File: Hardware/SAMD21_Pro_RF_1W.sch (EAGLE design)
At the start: 70 parts, among them J10 AVR_SPI_PROG_3X2TESTPOINTS, J12 5.5x2.1mm Barrel, J13 U.FL, J7 PTH, J9 External On/Off, Q1 310mA/60V/1.6Ω, U1 MCP73831, U3 3.3V, U4 ATSAMD21G, U5 4MB Flash, U6 E19-915MS1W, U7 ADJ5, U8 TXB0108DQSR, Y1 32.768kHz

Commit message: Stuff
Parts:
- R14: value 750K -> 750; device SparkFun-Resistors:750KOHM-0603-1/10W-1% -> SparkFun-Resistors:750OHM-0603-1/10W-1%
- R5: value 2.0k -> 2.2k; device SparkFun-Resistors:2.0KOHM-0603-1/10W-5% -> SparkFun-Resistors:2.2KOHM-0603-1/10W-1%
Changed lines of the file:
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@@
 <?xml version="1.0" encoding="utf-8"?>
 <!DOCTYPE eagle SYSTEM "eagle.dtd">
-<eagle version="9.0.1">
+<eagle version="9.1.3">
 <drawing>
 <settings>
@@
 <part name="GND10" library="supply1" library_urn="urn:adsk.eagle:library:371" deviceset="GND" device=""/>
 <part name="U1" library="SparkFun-IC-Power" deviceset="MCP73831" device=""/>
-<part name="R5" library="SparkFun-Resistors" deviceset="2.0KOHM" device="-0603-1/10W-5%" value="2.0k"/>
+<part name="R5" library="SparkFun-Resistors" deviceset="2.2KOHM" device="-0603-1/10W-1%" value="2.2k"/>
 <part name="GND14" library="supply1" library_urn="urn:adsk.eagle:library:371" deviceset="GND" device=""/>
 <part name="GND17" library="supply1" library_urn="urn:adsk.eagle:library:371" deviceset="GND" device=""/>
@@
 <part name="U7" library="SparkFun-IC-Power" deviceset="V_REG_LM1117" device="SOT223" value="ADJ5"/>
 <part name="F1" library="SparkFun-Fuses" deviceset="PPTC" device="_6V500MA" value="6V 0.5A"/>
-<part name="R14" library="SparkFun-Resistors" deviceset="750KOHM" device="-0603-1/10W-1%" value="750K"/>
+<part name="R14" library="SparkFun-Resistors" deviceset="750OHM" device="-0603-1/10W-1%" value="750"/>
 <part name="R15" library="SparkFun-Resistors" deviceset="240OHM" device="-0603-1/10W-1%" value="240"/>
 <part name="GND33" library="SparkFun" deviceset="GND" device=""/>

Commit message: Finalizing things
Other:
- note added: "Max Voltage Input: 7VDC"
- note removed: "Max Voltage Input: 20VDC"
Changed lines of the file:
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@@
 <text x="76.2" y="86.36" size="2.54" layer="94" font="vector">RX/TX LEDs</text>
 <text x="388.62" y="226.06" size="1.778" layer="97" font="vector" rot="R180">Reset occurs when low</text>
-<text x="218.44" y="274.32" size="1.778" layer="97" font="vector">Max Voltage Input: 20VDC</text>
+<text x="218.44" y="274.32" size="1.778" layer="97" font="vector">Max Voltage Input: 7VDC</text>
 <text x="218.44" y="271.78" size="1.778" layer="97" font="vector">Max Current Output: 800mA</text>
 <wire x1="294.64" y1="144.78" x2="294.64" y2="218.44" width="0.2032" layer="97" style="shortdash"/>
@@
 <text x="299.72" y="210.82" size="2.54" layer="94" font="vector">Level Shifters</text>
 <text x="160.02" y="256.54" size="1.27" layer="97">VIN 7-15V</text>
+<text x="190.5" y="93.98" size="1.778" layer="97" font="vector">Max Voltage Input: 7VDC</text>
 </plain>
 <instances>

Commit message: x02
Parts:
- removed J15, J2: (no value), SparkFun-Connectors:QWIIC_CONNECTORJS-1MM
- removed LED1: RED, SparkFun-LED:LED-RED0603
- removed R15: 240, SparkFun-Resistors:240OHM-0603-1/10W-1%
- removed R16: 10k, SparkFun-Resistors:10KOHM-0603-1/10W-1%
- removed S3: MOMENTARY-SWITCH-SPST-SMD-RIGHT-ANGLE, SparkFun-Switches:MOMENTARY-SWITCH-SPST-SMD-RIGHT-ANGLE
- removed U$26: SPECIAL_INSTRUCTIONS-ORDERING, SparkFun-Aesthetics:SPECIAL_INSTRUCTIONS-ORDERING
- removed U7: ADJ5, SparkFun-IC-Power:V_REG_LM1117SOT223
- removed U8: TXB0108DQSR, SparkFun-IC-Comms:TXB0108
- added D2: Green, SparkFun-LED:LED-GREEN0603
- added J14: CORTEX_DEBUG_PTH, SparkFun-Connectors:CORTEX_DEBUG_PTH
- added Q2: 310mA/60V/1.6Ω, SparkFun-DiscreteSemi:MOSFET-NCH-2N7002PW
- added R11: 10k, SparkFun-Resistors:10KOHM-0603-1/10W-1%
- added R3, R4: 1k, SparkFun-Resistors:1KOHM-0603-1/10W-1%
- added S2: Power, SparkFun-Switches:SWITCH-SPDT-SMD-RIGHT-ANGLE
- added U2: 3.3V, SparkFun-IC-Power:V_REG_AP2112K-3.3V
- C1: value 10uF -> 15pF; device SparkFun-Capacitors:10UF-POLAR-EIA3216-16V-10%(TANT) -> SparkFun-Capacitors:15PF-0603-50V-5%
- C10: value 0.1uF -> 10uF; device SparkFun-Capacitors:0.1UF-0603-25V-(+80/-20%) -> SparkFun-Capacitors:10UF-POLAR-EIA3216-16V-10%(TANT)
- C11, C14: value 0.1uF -> 1.0uF; device SparkFun-Capacitors:0.1UF-0603-25V-(+80/-20%) -> SparkFun-Capacitors:1.0UF-0603-16V-10%
- C12: value 1.0uF -> 10uF; device SparkFun-Capacitors:1.0UF-0603-16V-10% -> SparkFun-Capacitors:10UF-POLAR-EIA3216-16V-10%(TANT)
- C13, C7: value 10uF -> 0.1uF; device SparkFun-Capacitors:10UF-POLAR-EIA3216-16V-10%(TANT) -> SparkFun-Capacitors:0.1UF-0603-25V-(+80/-20%)
- C3: value 15pF -> 0.1uF; device SparkFun-Capacitors:15PF-0603-50V-5% -> SparkFun-Capacitors:0.1UF-0603-25V-(+80/-20%)
- C5: value 1.0uF -> 0.1uF; device SparkFun-Capacitors:1.0UF-0603-16V-10% -> SparkFun-Capacitors:0.1UF-0603-25V-(+80/-20%)
- C8: value 0.1uF -> 4.7uF; device SparkFun-Capacitors:0.1UF-0603-25V-(+80/-20%) -> SparkFun-Capacitors:4.7UF-0603-6.3V-(10%)
- C9: value 4.7uF -> 10uF; device SparkFun-Capacitors:4.7UF-0603-6.3V-(10%) -> SparkFun-Capacitors:10UF-POLAR-EIA3216-16V-10%(TANT)
- D1: value Green -> Yellow; device SparkFun-LED:LED-GREEN0603 -> SparkFun-LED:LED-YELLOW0603
- D3: value 3A/10V/300mV -> BLUE; device SAMD21_ProRF_1W:DIODE-SCHOTTKY-BAT60A -> SparkFun-LED:LED-BLUE0603
- D4: value BLUE -> 3A/10V/300mV; device SparkFun-LED:LED-BLUE0603 -> SAMD21_ProRF_1W:DIODE-SCHOTTKY-BAT60A
- D6: value Yellow -> RED; device SparkFun-LED:LED-YELLOW0603 -> SparkFun-LED:LED-RED0603
- J10: value AVR_SPI_PROG_3X2TESTPOINTS -> (none); device SparkFun-Connectors:AVR_SPI_PROG_3X2TESTPOINTS -> SparkFun-Connectors:CONN_10NO_SILK_PTH_FEMALE
- J11: device SparkFun-Connectors:CONN_09NO_SILK -> SparkFun-Connectors:QWIIC_CONNECTORJS-1MM
- J12: value 5.5x2.1mm Barrel -> (none); device SparkFun-Connectors:POWER_JACKSMD -> SparkFun-Connectors:CONN_01PTH_NO_SILK_YES_STOP
- J13: value U.FL -> (none); device SparkFun-Connectors:U.FL -> SparkFun-Connectors:QWIIC_CONNECTORJS-1MM
- J3: value (none) -> PTH; device SparkFun-Connectors:CONN_10NO_SILK_PTH_FEMALE -> SparkFun-Connectors:CONN_021X02_NO_SILK
- J4: device SparkFun-Connectors:CONN_01PTH_NO_SILK_YES_STOP -> SparkFun-Connectors:CONN_021X02_NO_SILK
- J5: value (none) -> 5.5x2.1mm Barrel; device SparkFun-Connectors:CONN_09NO_SILK -> SparkFun-Connectors:POWER_JACKSMD
- J7: value PTH -> (none); device SparkFun-Connectors:CONN_021X02_NO_SILK -> SparkFun-Connectors:CONN_09NO_SILK
- J8: value (none) -> External On/Off
- J9: value External On/Off -> (none); device SparkFun-Connectors:CONN_021X02_NO_SILK -> SparkFun-Connectors:CONN_09NO_SILK
- R10, R7, R9: value 1k -> 10k; device SparkFun-Resistors:1KOHM-0603-1/10W-1% -> SparkFun-Resistors:10KOHM-0603-1/10W-1%
- R13: value 1k -> 2.2k; device SparkFun-Resistors:1KOHM-0603-1/10W-1% -> SparkFun-Resistors:2.2KOHM-0603-1/10W-1%
- R14: value 750 -> 2.2k; device SparkFun-Resistors:750OHM-0603-1/10W-1% -> SparkFun-Resistors:2.2KOHM-0603-1/10W-1%
- R2, R8: value 10k -> 1k; device SparkFun-Resistors:10KOHM-0603-1/10W-1% -> SparkFun-Resistors:1KOHM-0603-1/10W-1%
- R5: value 2.2k -> 240; device SparkFun-Resistors:2.2KOHM-0603-1/10W-1% -> SparkFun-Resistors:240OHM-0603-1/10W-1%
- R6: value 10k -> 750; device SparkFun-Resistors:10KOHM-0603-1/10W-1% -> SparkFun-Resistors:750OHM-0603-1/10W-1%
- S1: value Power -> MOMENTARY-SWITCH-SPST-SMD-5.2-REDUNDANT; device SparkFun-Switches:SWITCH-SPDT-SMD-RIGHT-ANGLE -> SparkFun-Switches:MOMENTARY-SWITCH-SPST-SMD-5.2-REDUNDANT
- U1: value MCP73831 -> ATSAMD21G; device SparkFun-IC-Power:MCP73831 -> temp:ATSAMD21G
- U3: value 3.3V -> ADJ5; device SparkFun-IC-Power:V_REG_AP2112K-3.3V -> SparkFun-IC-Power:V_REG_LM1117SOT223
- U4: value ATSAMD21G -> 4MB Flash; device temp:ATSAMD21G -> SparkFun-IC-Memory:AT25SF041
- U5: value 4MB Flash -> E19-915MS1W; device SparkFun-IC-Memory:AT25SF041 -> SAMD21_ProRF_1W:E19-915MS1W
- U6: value E19-915MS1W -> TXB0108DQSR; device SAMD21_ProRF_1W:E19-915MS1W -> SparkFun-IC-Comms:TXB0108
- renumbered FRAME2 to FRAME1
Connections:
- removed net CHARGE_STAT: R9.1, U1.STAT
- removed net D2: J3.6, U4.PA14(XIN/SER2:2+)_D2
- removed net D3: J3.5, U4.PA09(I2C/AIN17/SER0:1+)_D3
- removed net D4: J3.4, U4.PA08(I2C/AIN16/SER0:0+)_D4
- removed net E19_RST: U4.PA17(I2C/SER1:1+)_D13, U6.!RST
- removed net N$11: R5.1, U1.PROG
- removed net N$8: D4.C, R9.2
- removed net N$9: J9.2, S1.O
- removed net VBATT_LVL: R1.1, R2.2, U4.A5_PB02(AIN10/SER5:0)
- new net !E19_RST: Q1.S, R9.1, U1.PA13(I2C/SER2:1+)
- new net !E19_RST5V: Q1.D, R11.1, U5.!RST
- new net D13: R4.2, U1.PA17(I2C/SER1:1+)_D13
- new net EEPROM_MISO: J6.6, U1.PA14(XIN/SER2:2+)_D2, U4.SO(D1)
- new net EEPROM_MOSI: J6.4, U1.PA08(I2C/AIN16/SER0:0+)_D4, U4.SI(D0)
- new net EEPROM_SCLK: J6.5, U1.PA09(I2C/AIN17/SER0:1+)_D3, U4.SCK
- new net N$3: D3.A, R4.1
- net !E19_CS: now also Q2.S, R10.1, U1.PA19(SER1:3+)_D12; no longer Q1.S, R12.1, U4.PA19(SER1:3+)_D12
- net !E19_CS5V: now also Q2.D, R12.1, U5.!NSS; no longer Q1.D, R16.1, U6.!NSS
- net !RST: now also J14.!RESET, J6.8, R1.1, S1.2, U1.!RESET!; no longer J10.5, J3.8, R6.1, S3.1, U4.!RESET!
- net 3.3V: now also C10.+, C11.1, C13.2, C5.2, D2.A, J11.2, J13.2, J14.VCC, J6.2, Q2.G, R1.2, R10.2, R14.2, R7.2, R9.2, U1.VDDCORE, U1.VDDIN, U1.VDDIO@17, U1.VDDIO@36, U2.OUT, U4.!HOLD(D3), U4.!WP(D2), U4.VCC, U6.OE, U6.VCCA; no longer C10.2, C12.1, C13.+, C14.2, D6.A, J10.2, J15.2, J2.2, J3.2, R12.2, R6.2, U3.OUT, U4.VDDCORE, U4.VDDIN, U4.VDDIO@17, U4.VDDIO@36, U5.!HOLD(D3), U5.!WP(D2), U5.VCC, U8.OE, U8.VCCA
- net 5V: now also C12.+, C14.1, C15.2, D4.C, R11.2, R12.2, U2.EN, U2.IN, U5.VCC, U6.VCCB; no longer C5.1, C7.+, C8.2, D3.C, R16.2, U3.EN, U3.IN, U6.VCC, U8.VCCB
- net A0: now also J7.9, U1.A0_PA02(AIN0/DAC); no longer J11.9, U4.A0_PA02(AIN0/DAC)
- net A1: now also J7.8, U1.A1_PB08(AIN2/SER4:0/TC4:0); no longer J11.8, U4.A1_PB08(AIN2/SER4:0/TC4:0)
- net A2: now also J7.7, U1.A2_PB09(AIN3/SER4:1/TC4:1); no longer J11.7, U4.A2_PB09(AIN3/SER4:1/TC4:1)
- net A3: now also J7.6, U1.A3_PA04(AIN4/REFB/SER0:0/TC0:0); no longer J11.6, U4.A3_PA04(AIN4/REFB/SER0:0/TC0:0)
- net A4: now also J7.5, U1.A4_PA05(AIN5/SER0:1/TC0:1); no longer J11.5, U4.A4_PA05(AIN5/SER0:1/TC0:1)
- net ANT: now also J12.1, U5.ANT; no longer J13.SIGNAL, J4.1, U6.ANT
- net D+: now also U1.PA25(SER3:3+); no longer U4.PA25(SER3:3+)
- net D-: now also U1.PA24(SER3:2+); no longer U4.PA24(SER3:2+)
- net D10: now also U1.PA18(SER1:2+)_D10, U6.A7; no longer U4.PA18(SER1:2+)_D10, U8.A7
- net D11: now also U1.PA16(I2C/SER1:0+)_D11, U6.A8; no longer U4.PA16(I2C/SER1:0+)_D11, U8.A8
- net D5: now also J6.7, U1.PA15(XOUT/SER2:3+)_D5; no longer J3.7, U4.PA15(XOUT/SER2:3+)_D5
- net D8_!FLASH_CS: now also R7.1, U1.D8_PA06(AIN6/SER0:2/TC1:0), U4.!CS; no longer R8.1, U4.D8_PA06(AIN6/SER0:2/TC1:0), U5.!CS
- net D9: now also J6.3, U1.D9_PA07(AIN7/SER0:3/TC1:1); no longer J3.3, U4.D9_PA07(AIN7/SER0:3/TC1:1)
- net DIO05V: now also U5.DIO0, U6.B6; no longer U6.DIO0, U8.B6
- net DIO15V: now also U5.DIO1, U6.B7; no longer U6.DIO1, U8.B7
- net DIO25V: now also U5.DIO2, U6.B8; no longer U6.DIO2, U8.B8
- net E19_INT: now also U1.PA20(SER5:2+)_D6, U6.A6; no longer U4.PA20(SER5:2+)_D6, U8.A6
- net E19_RXEN: now also U1.PB23(SER5:3+), U6.A5; no longer U4.PB23(SER5:3+), U8.A5
- net E19_RXEN5V: now also U5.RXEN, U6.B5; no longer U6.RXEN, U8.B5
- net E19_TXEN: now also U1.PB22(SER5:2+), U6.A4; no longer U4.PB22(SER5:2+), U8.A4
- net E19_TXEN5V: now also U5.TXEN, U6.B4; no longer U6.TXEN, U8.B4
- net GND: now also C1.1, C10.-, C11.2, C12.-, C13.1, C14.2, C5.1, C7.1, C8.2, C9.-, D3.C, D6.C, J10.1, J10.10, J10.2, J10.3, J10.4, J10.5, J10.7, J10.8, J10.9, J13.1, J14.GND@3, J14.GND@5, J3.1, J4.1, J5.GND, J5.GNDBREAK, J9.1, J9.2, J9.3, J9.4, J9.5, J9.6, J9.7, J9.8, J9.9, R6.1, S1.1, U1.GND@18, U1.GND@35, U1.GND@42, U1.GNDANA, U2.GND, U4.GND; no longer C1.-, C10.1, C11.1, C12.2, C13.-, C14.1, C5.2, C7.-, C8.1, C9.2, J12.GND, J12.GNDBREAK, J13.GND@0, J13.GND@1, J15.1, J2.1, J5.1, J5.2, J5.3, J5.4, J5.5, J5.6, J5.7, J5.8, J5.9, J6.1, J6.10, J6.2, J6.3, J6.4, J6.5, J6.6, J6.7, J6.8, J6.9, J8.1, LED1.C, R14.1, R2.1, R5.2, S3.2, U1.VSS, U3.GND, U4.GND@18, U4.GND@35, U4.GND@42, U4.GNDANA, U8.GND
- net MISO: now also J14.SWO/TDO, J7.2, U1.PA12(I2C/SER2:0+)_MISO, U6.A2; no longer J10.1, J11.2, U4.PA12(I2C/SER2:0+)_MISO, U5.SO(D1), U8.A2
- net MISO5V: now also U5.MISO, U6.B2; no longer U6.MISO, U8.B2
- net MOSI: now also J7.3, U1.PB10(SER4:2+)_MOSI, U6.A3; no longer J11.3, U4.PB10(SER4:2+)_MOSI, U5.SI(D0), U8.A3
- net MOSI5V: now also U5.MOSI, U6.B3; no longer U6.MOSI, U8.B3
- net N$1: now also D1.C, R2.2; no longer D6.C, R10.2
- net N$12: now also D4.A; no longer D3.A
- net N$13: now also R5.1, R6.2, U3.ADJ; no longer R14.2, R15.1, U7.ADJ
- net N$14: now also R5.2, U3.OUT, U3.OUT@1; no longer R15.2, U7.OUT, U7.OUT@1
- net N$2: now also D2.C, R3.2; no longer D1.C, R7.2
- net N$38: now also D6.A, R8.1; no longer LED1.A, R13.1
- net N$6: now also C1.2, U1.PA00(XIN32/SER1:0/TC2:0); no longer C2.2, U4.PA00(XIN32/SER1:0/TC2:0)
- net N$7: now also C2.2, U1.PA01(XOUT32/SER1:1/TC2:1); no longer C3.2, U4.PA01(XOUT32/SER1:1/TC2:1)
- net RAW: now also J6.1, J8.1, S2.P, U3.IN; no longer J3.1, J9.1, S1.P, U7.IN
- net RXI: now also J6.10, U1.PA11(AIN19/SER0:3+)_D0/RX; no longer J3.10, U4.PA11(AIN19/SER0:3+)_D0/RX
- net RX_LED: now also R2.1, U1.PB03(AIN11/SER5:1); no longer R10.1, U4.PB03(AIN11/SER5:1)
- net SCK: now also J7.4, U1.PB11(SER4:3+)_SCK, U6.A1; no longer J11.4, U4.PB11(SER4:3+)_SCK, U5.SCK, U8.A1
- net SCK5V: now also U5.SCK, U6.B1; no longer U6.SCK, U8.B1
- net SCL: now also J11.4, J13.4, R14.1, U1.PA23(I2C/SER3:0+)_SCL; no longer J15.4, J2.4, U4.PA23(I2C/SER3:0+)_SCL
- net SDA: now also J11.3, J13.3, R13.1, U1.PA22(I2C/SER3:0+)_SDA; no longer J15.3, J2.3, U4.PA22(I2C/SER3:0+)_SDA
- net SWDCLK: now also J14.SWDCLK/TCK, U1.PA30(SWCLK/SER1:2+); no longer J10.3, U4.PA30(SWCLK/SER1:2+)
- net SWDIO: now also J14.SWDIO/TMS, U1.PA31(SWDIO/SER1:3+); no longer J10.4, U4.PA31(SWDIO/SER1:3+)
- net TXO: now also J6.9, U1.PA10(AIN18/SER0:2+)_D1/TX; no longer J3.9, U4.PA10(AIN18/SER0:2+)_D1/TX
- net TX_LED: now also R3.1, U1.PA27; no longer R7.1, U4.PA27
- net USB_VCC: now also C3.2, C8.1, J4.2; no longer C11.2, C9.1, D4.A, J8.2, U1.VIN
- net VBATT: now also C9.+, J3.2, J5.PWR, J8.2, S2.S; no longer C1.+, J12.PWR, J7.2, R1.2, S1.S, U1.VBAT
- net VDDANA: now also C7.2, U1.VDDANA; no longer C15.2, U4.VDDANA
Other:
- note added: "D2"
- note added: "D3"
- note added: "D4"
- note added: "Max Current Output: 600mA"
- note added: "Max Voltage Input: 15VDC"
- note added: "Max Voltage Input: 6VDC"
- note added: "VUSB"
- note added: "When not using EEPROM you can use these pins as GPIOs D2-D4"
- note added: "x02"
- note removed: "Antenna"
- note removed: "LIPO CHARGER"
- note removed: "Reset occurs when low"
- note removed: "x01"
- moved on the sheet: C11, C14, C15, C2, C3, C4, C5, C6, C8, D1, D6, J6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

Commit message: x02 ready for order
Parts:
- removed LOGO1: OSHW-LOGOMINI, SparkFun-Aesthetics:OSHW-LOGOMINI
- U$34: value SPARKX-LOGO2 -> SPARKX-LOGO4; device SparkX:SPARKX-LOGO2 -> SparkX:SPARKX-LOGO4
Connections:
- net GND: now also J14.GNDDTCT
- net MISO: no longer J14.SWO/TDO

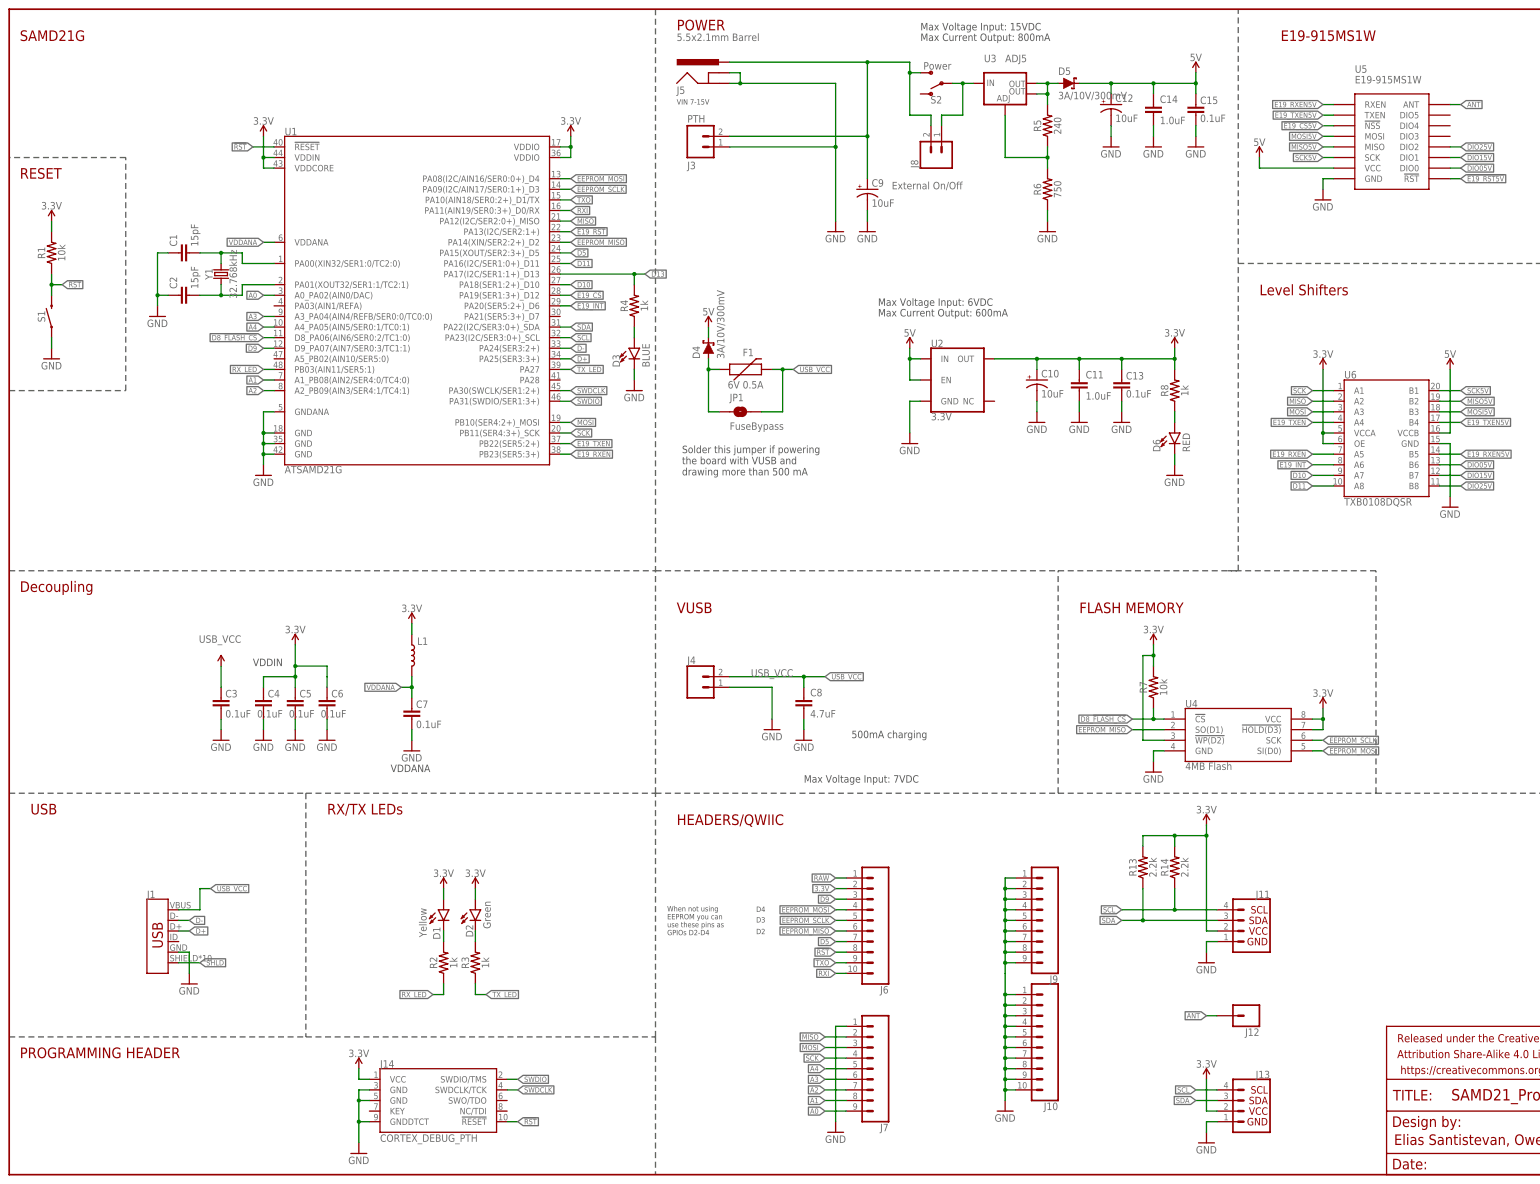
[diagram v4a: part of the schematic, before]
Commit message: Brought libraries into spec
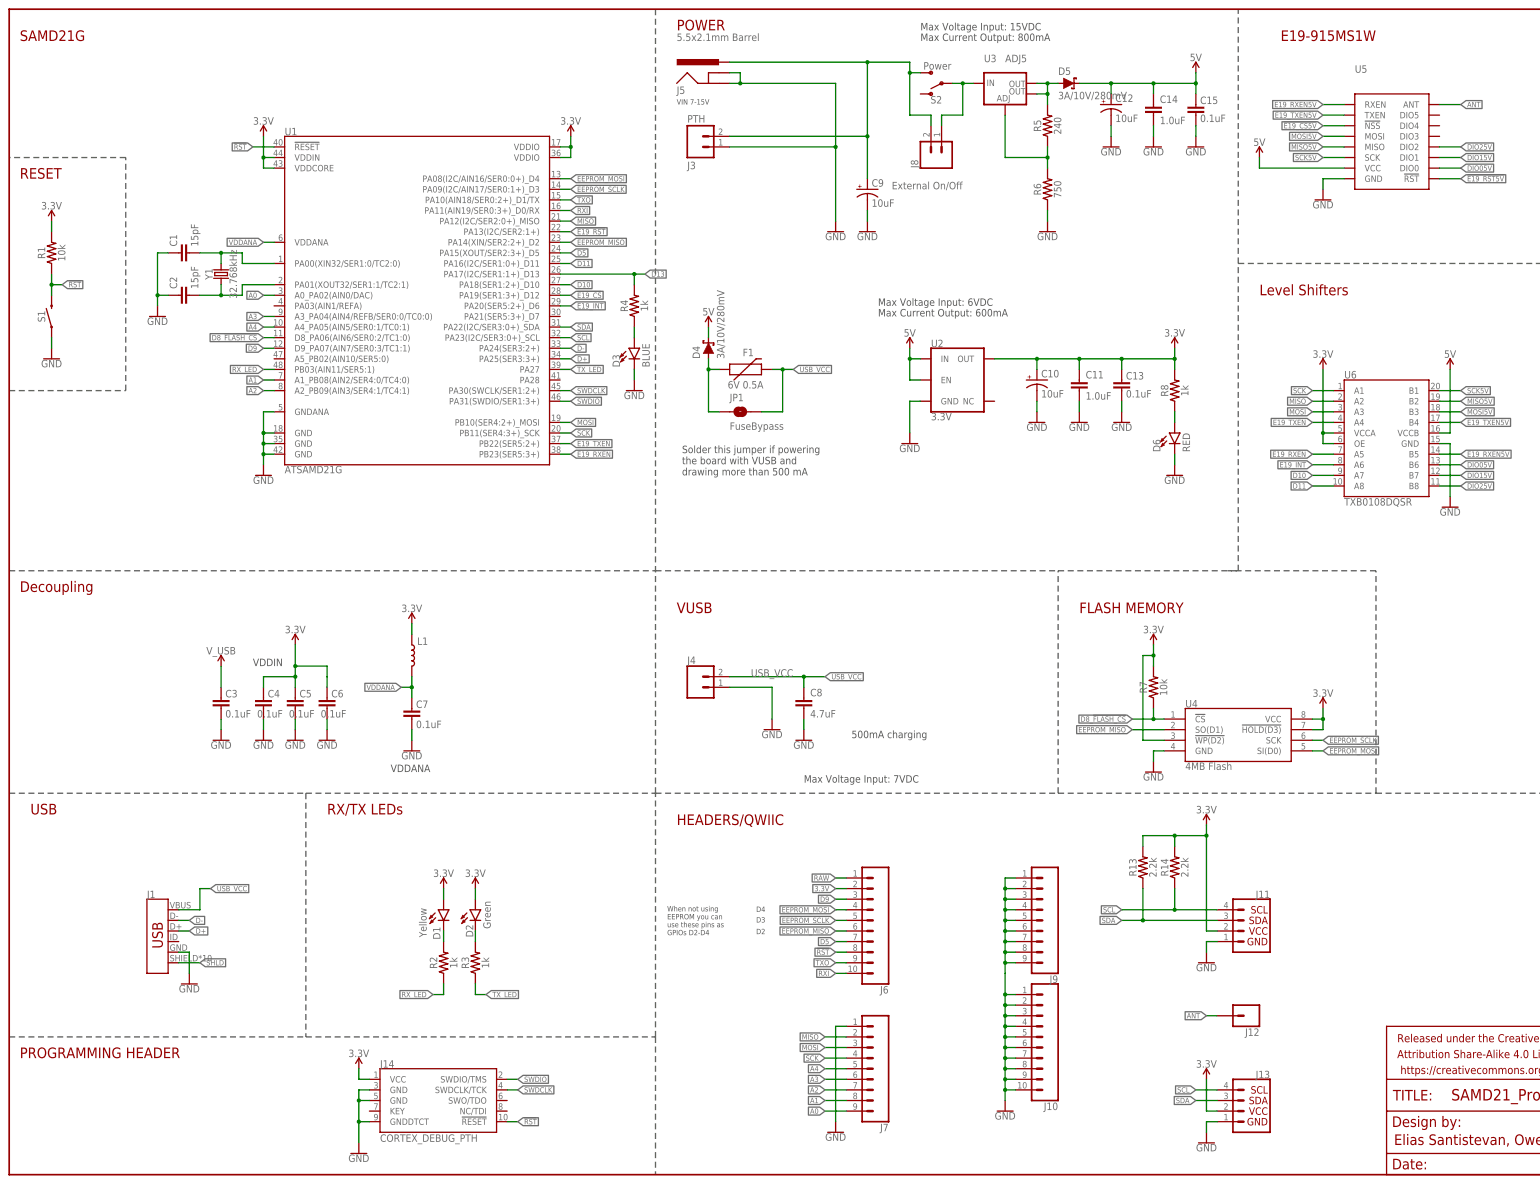
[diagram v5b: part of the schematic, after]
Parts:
- D4, D5: value 3A/10V/300mV -> 3A/10V/280mV; device SAMD21_ProRF_1W:DIODE-SCHOTTKY-BAT60A -> SparkFun-DiscreteSemi:DIODE-SCHOTTKY-BAT60A
- U1: device temp:ATSAMD21G -> SparkFun-IC-Microcontroller:ATSAMD21G
- U5: value E19-915MS1W -> (none); device SAMD21_ProRF_1W:E19-915MS1W -> SparkFun-RF:E19-915MS1W
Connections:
- new net V_USB: C3.2
- net USB_VCC: no longer C3.2

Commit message: Fixes
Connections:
- removed net USB_VCC: C8.1, F1.2, J1.VBUS, J4.2, JP1.2
- net V_USB: now also C8.1, F1.2, J1.VBUS, J4.2, JP1.2
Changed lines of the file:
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@@
 <part name="GND21" library="SparkFun-PowerSymbols" deviceset="GND" device=""/>
 <part name="GND23" library="SparkFun-PowerSymbols" deviceset="GND" device=""/>
+<part name="SUPPLY25" library="SparkFun-PowerSymbols" deviceset="V_USB" device=""/>
+<part name="SUPPLY26" library="SparkFun-PowerSymbols" deviceset="V_USB" device=""/>
+<part name="SUPPLY27" library="SparkFun-PowerSymbols" deviceset="V_USB" device=""/>
 </parts>
 <sheets>
@@
 <instance part="GND21" gate="1" x="256.54" y="180.34"/>
 <instance part="GND23" gate="1" x="266.7" y="180.34"/>
+<instance part="SUPPLY25" gate="G$1" x="45.72" y="68.58"/>
+<instance part="SUPPLY26" gate="G$1" x="187.96" y="195.58"/>
+<instance part="SUPPLY27" gate="G$1" x="190.5" y="121.92"/>
 </instances>
 <busses>
@@
 </segment>
 </net>
-<net name="USB_VCC" class="1">
-<segment>
-<wire x1="45.72" y1="63.5" x2="45.72" y2="68.58" width="0.1524" layer="91"/>
-<wire x1="45.72" y1="68.58" x2="48.26" y2="68.58" width="0.1524" layer="91"/>
-<label x="48.26" y="68.58" size="1.27" layer="95" font="vector" xref="yes"/>
-<wire x1="40.64" y1="63.5" x2="45.72" y2="63.5" width="0.1524" layer="91"/>
-<pinref part="J1" gate="J1" pin="VBUS"/>
-</segment>
-<segment>
-<pinref part="F1" gate="F1" pin="2"/>
-<wire x1="182.88" y1="193.04" x2="185.42" y2="193.04" width="0.1524" layer="91"/>
-<pinref part="JP1" gate="G$1" pin="2"/>
-<wire x1="180.34" y1="182.88" x2="185.42" y2="182.88" width="0.1524" layer="91"/>
-<wire x1="185.42" y1="182.88" x2="185.42" y2="193.04" width="0.1524" layer="91"/>
-<wire x1="185.42" y1="193.04" x2="187.96" y2="193.04" width="0.1524" layer="91"/>
-<junction x="185.42" y="193.04"/>
-<label x="187.96" y="193.04" size="1.27" layer="95" xref="yes"/>
-</segment>
-<segment>
-<wire x1="172.72" y1="119.38" x2="190.5" y2="119.38" width="0.1524" layer="91"/>
-<wire x1="190.5" y1="119.38" x2="195.58" y2="119.38" width="0.1524" layer="91"/>
-<wire x1="190.5" y1="116.84" x2="190.5" y2="119.38" width="0.1524" layer="91"/>
-<junction x="190.5" y="119.38"/>
-<label x="177.8" y="119.38" size="1.778" layer="95" font="vector"/>
-<pinref part="C8" gate="G$1" pin="1"/>
-<pinref part="J4" gate="G$1" pin="2"/>
-<label x="195.58" y="119.38" size="1.27" layer="95" xref="yes"/>
-</segment>
-</net>
 <net name="3.3V" class="1">
 <segment>
@@
 <pinref part="SUPPLY4" gate="G$1" pin="V_USB"/>
 </segment>
-</net>
+<segment>
+<wire x1="45.72" y1="63.5" x2="45.72" y2="68.58" width="0.1524" layer="91"/>
+<wire x1="40.64" y1="63.5" x2="45.72" y2="63.5" width="0.1524" layer="91"/>
+<pinref part="J1" gate="J1" pin="VBUS"/>
+<pinref part="SUPPLY25" gate="G$1" pin="V_USB"/>
+</segment>
+<segment>
+<pinref part="F1" gate="F1" pin="2"/>
+<wire x1="182.88" y1="193.04" x2="185.42" y2="193.04" width="0.1524" layer="91"/>
+<pinref part="JP1" gate="G$1" pin="2"/>
+<wire x1="180.34" y1="182.88" x2="185.42" y2="182.88" width="0.1524" layer="91"/>
+<wire x1="185.42" y1="182.88" x2="185.42" y2="193.04" width="0.1524" layer="91"/>
+<wire x1="185.42" y1="193.04" x2="187.96" y2="193.04" width="0.1524" layer="91"/>
+<junction x="185.42" y="193.04"/>
+<pinref part="SUPPLY26" gate="G$1" pin="V_USB"/>
+<wire x1="187.96" y1="193.04" x2="187.96" y2="195.58" width="0.1524" layer="91"/>
+</segment>
+<segment>
+<wire x1="172.72" y1="119.38" x2="190.5" y2="119.38" width="0.1524" layer="91"/>
+<wire x1="190.5" y1="116.84" x2="190.5" y2="119.38" width="0.1524" layer="91"/>
+<label x="177.8" y="119.38" size="1.778" layer="95" font="vector"/>
+<pinref part="C8" gate="G$1" pin="1"/>
+<pinref part="J4" gate="G$1" pin="2"/>
+<pinref part="SUPPLY27" gate="G$1" pin="V_USB"/>
+<wire x1="190.5" y1="121.92" x2="190.5" y2="119.38" width="0.1524" layer="91"/>
+<junction x="190.5" y="119.38"/>
+</segment>
+</net>
